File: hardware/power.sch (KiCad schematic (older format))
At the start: 22 parts

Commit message: Almost finished layout
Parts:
- removed D? (x3): 1N4002, symbol D_Small
- added D4, D5, D6: S1KB-13-F, Diodes_SMD:SMB_Standard, symbol D_Small
- added D7: LED_5V, Connectors_Molex:Molex_KK-6410-02_02x2.54mm_Straight, symbol Led_Small
- added D8: LED_3V3, Connectors_Molex:Molex_KK-6410-02_02x2.54mm_Straight, symbol Led_Small
- added R35: 270R, Resistors_SMD:R_1210, symbol R_Small
- added R36: 180R, Resistors_SMD:R_1210, symbol R_Small
- C34, C37, C38, C41: renamed from C?; value 47u -> 10u; footprint (none) -> Capacitors_ThroughHole:C_Radial_D5_L11_P2
- C35, C39: renamed from C?; footprint (none) -> Capacitors_SMD:C_1210
- C36, C40: renamed from C?; value ? -> 10u; footprint (none) -> Capacitors_ThroughHole:C_Radial_D5_L11_P2
- D3: renamed from D?; value 1N4002 -> S1KB-13-F; footprint (none) -> Diodes_SMD:SMB_Standard
- R31, R32, R33, R34: renamed from R?; footprint (none) -> Resistors_SMD:R_1210
- U4, U5: renamed from U?; footprint TO_SOT_Packages_THT:TO-220_Neutral123_Vertical_LargePads -> TO_SOT_Packages_THT:TO-220_Neutral123_Vertical_MountedFromLS
- gave numbers to parts that had none: 4
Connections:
- net 3V3A: now also D5.2 (A), D6.1 (K), D8.2 (A)
- net 5VA: now also D4.1 (K), D5.1 (K), D7.2 (A)
- net GND: now also R35.2, R36.2
- net at C40.1, R33.2, R34.1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: now also D6.2 (A)
- net at C36.1, R31.2, R32.1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: now also D4.2 (A)
- new net: D7.1 (K), R35.1
- new net: D8.1 (K), R36.1

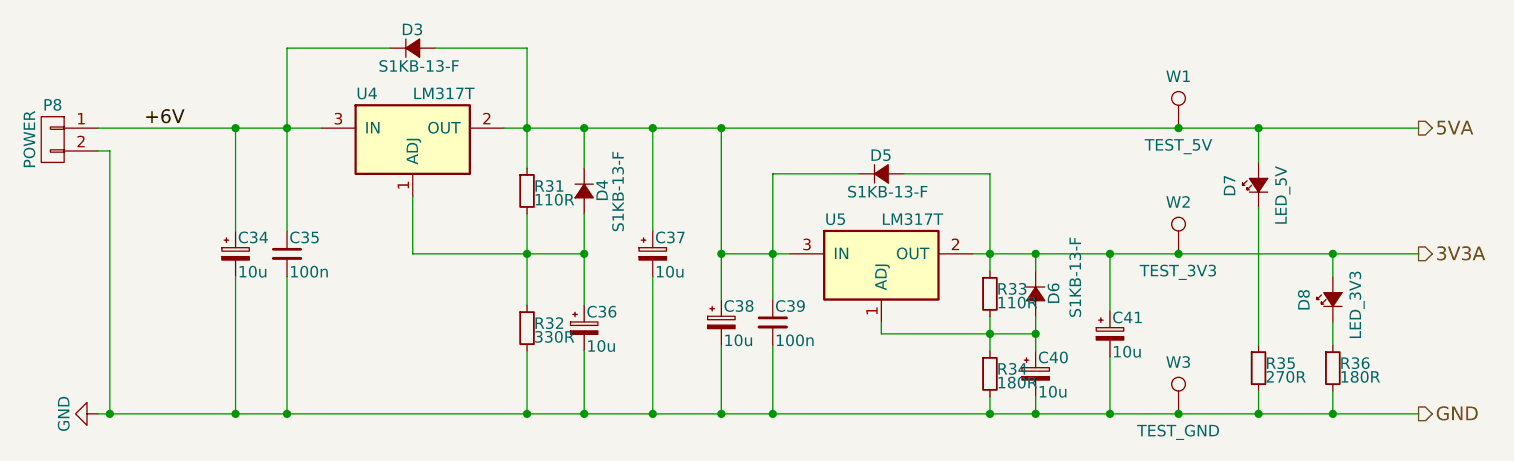
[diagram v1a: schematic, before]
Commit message: Move labels, replace some SMB diodes with SMA, final tweaks
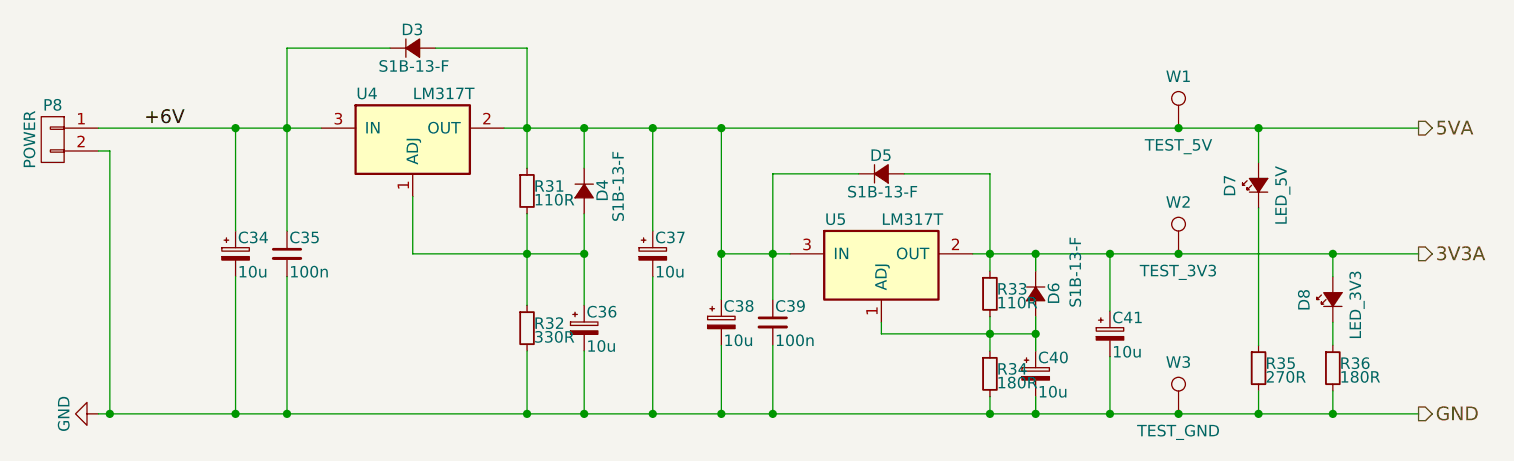
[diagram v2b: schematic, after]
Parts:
- D3, D4, D5, D6: value S1KB-13-F -> S1B-13-F; footprint Diodes_SMD:SMB_Standard -> Diodes_SMD:SMA_Standard
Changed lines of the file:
@@
 P 4750 2800
 F 0 "D3" H 4700 2880 50  0000 L CNN
-F 1 "S1KB-13-F" H 4600 2720 50  0000 L CNN
-F 2 "Diodes_SMD:SMB_Standard" V 4750 2800 50  0001 C CNN
+F 1 "S1B-13-F" H 4600 2720 50  0000 L CNN
+F 2 "Diodes_SMD:SMA_Standard" V 4750 2800 50  0001 C CNN
 F 3 "" V 4750 2800 50  0000 C CNN
 	1    4750 2800
@@
 P 6800 3350
 F 0 "D5" H 6750 3430 50  0000 L CNN
-F 1 "S1KB-13-F" H 6650 3270 50  0000 L CNN
-F 2 "Diodes_SMD:SMB_Standard" V 6800 3350 50  0001 C CNN
+F 1 "S1B-13-F" H 6650 3270 50  0000 L CNN
+F 2 "Diodes_SMD:SMA_Standard" V 6800 3350 50  0001 C CNN
 F 3 "" V 6800 3350 50  0000 C CNN
 	1    6800 3350
@@
 P 5500 3425
 F 0 "D4" H 5450 3505 50  0000 L CNN
-F 1 "S1KB-13-F" H 5325 3575 50  0000 L CNN
-F 2 "Diodes_SMD:SMB_Standard" V 5500 3425 50  0001 C CNN
+F 1 "S1B-13-F" H 5325 3575 50  0000 L CNN
+F 2 "Diodes_SMD:SMA_Standard" V 5500 3425 50  0001 C CNN
 F 3 "" V 5500 3425 50  0000 C CNN
 	1    5500 3425
@@
 P 7475 3875
 F 0 "D6" H 7425 3955 50  0000 L CNN
-F 1 "S1KB-13-F" H 7225 4050 50  0000 L CNN
-F 2 "Diodes_SMD:SMB_Standard" V 7475 3875 50  0001 C CNN
+F 1 "S1B-13-F" H 7225 4050 50  0000 L CNN
+F 2 "Diodes_SMD:SMA_Standard" V 7475 3875 50  0001 C CNN
 F 3 "" V 7475 3875 50  0000 C CNN
 	1    7475 3875

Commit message: Move LM317 regulator footprints to underside; final tweaks
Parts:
- U4, U5: footprint TO_SOT_Packages_THT:TO-220_Neutral123_Vertical_MountedFromLS -> TO_SOT_Packages_THT:TO-220_Neutral123_Vertical
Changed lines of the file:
@@
 F 0 "U5" H 6600 3950 50  0000 C CNN
 F 1 "LM317T" H 6800 3950 50  0000 L CNN
-F 2 "TO_SOT_Packages_THT:TO-220_Neutral123_Vertical_MountedFromLS" H 6800 3850 50  0001 C CIN
+F 2 "TO_SOT_Packages_THT:TO-220_Neutral123_Vertical" H 6800 3850 50  0001 C CIN
 F 3 "" H 6800 3750 50  0000 C CNN
 	1    6800 3750
@@
 F 0 "U4" H 4550 3400 50  0000 C CNN
 F 1 "LM317T" H 4750 3400 50  0000 L CNN
-F 2 "TO_SOT_Packages_THT:TO-220_Neutral123_Vertical_MountedFromLS" H 4750 3300 50  0001 C CIN
+F 2 "TO_SOT_Packages_THT:TO-220_Neutral123_Vertical" H 4750 3300 50  0001 C CIN
 F 3 "" H 4750 3200 50  0000 C CNN
 	1    4750 3200

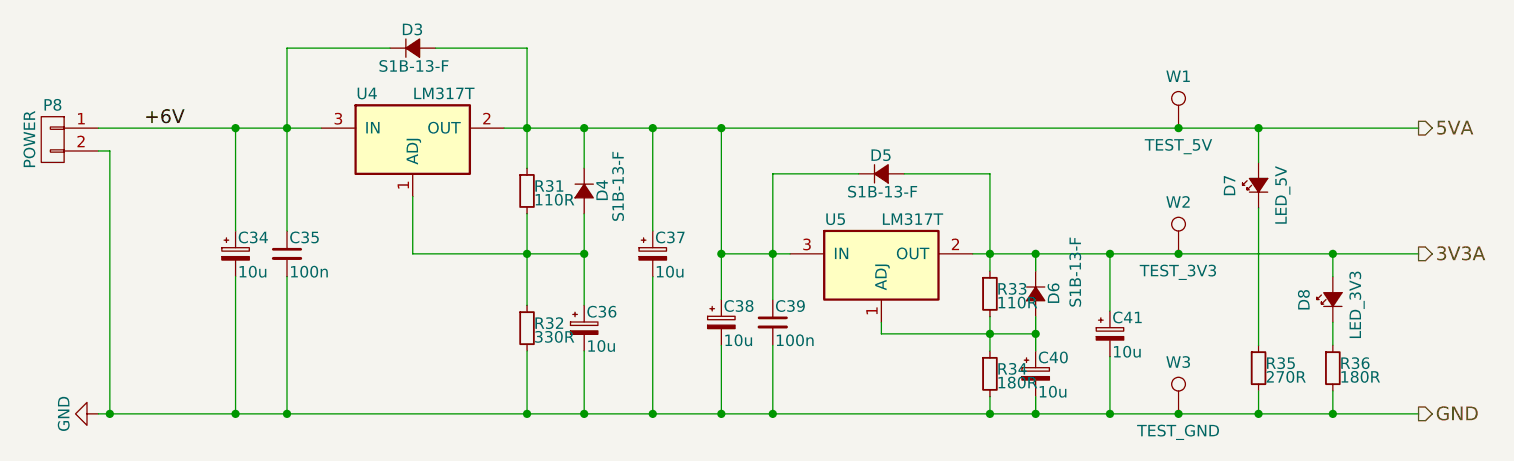
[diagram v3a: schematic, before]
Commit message: Revision of board to address issues
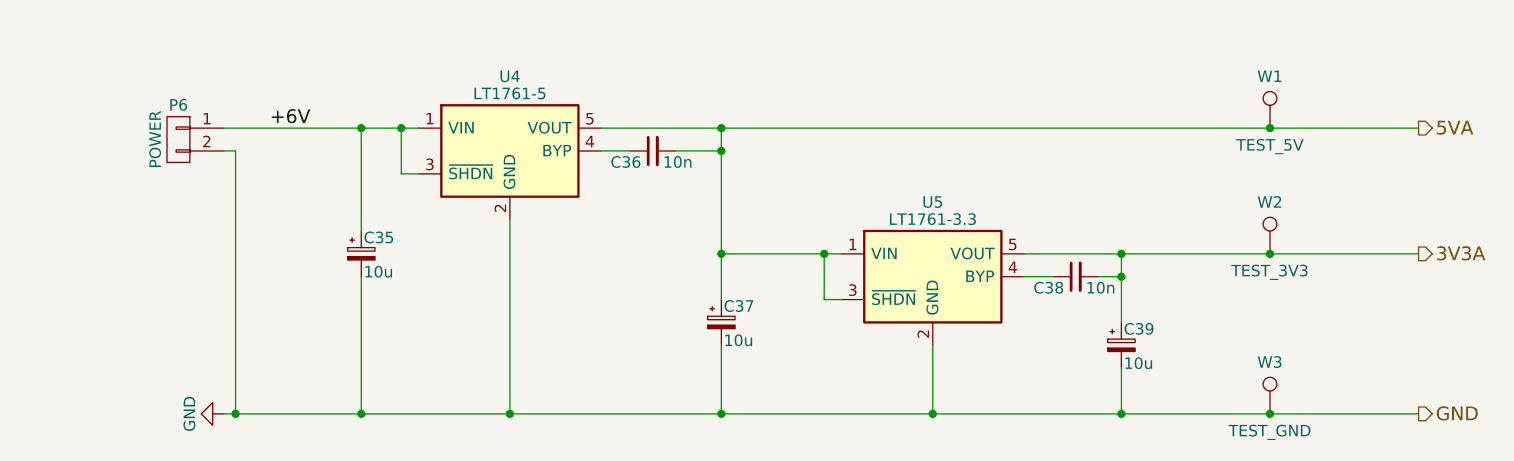
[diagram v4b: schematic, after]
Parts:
- removed C35, C39: 100n, Capacitors_SMD:C_1210, symbol C_Small
- removed C36, C37, C40, C41: 10u, Capacitors_ThroughHole:C_Radial_D5_L11_P2, symbol CP_Small
- removed D3, D4, D5, D6: S1B-13-F, Diodes_SMD:SMA_Standard, symbol D_Small
- removed D7: LED_5V, Connectors_Molex:Molex_KK-6410-02_02x2.54mm_Straight, symbol Led_Small
- removed D8: LED_3V3, Connectors_Molex:Molex_KK-6410-02_02x2.54mm_Straight, symbol Led_Small
- removed R31, R33: 110R, Resistors_SMD:R_1210, symbol R_Small
- removed R32: 330R, Resistors_SMD:R_1210, symbol R_Small
- removed R34, R36: 180R, Resistors_SMD:R_1210, symbol R_Small
- removed R35: 270R, Resistors_SMD:R_1210, symbol R_Small
- removed U4, U5: LM317T, TO_SOT_Packages_THT:TO-220_Neutral123_Vertical, symbol LM317T
- added C36, C38: 10n, Capacitors_SMD:C_1206, symbol C_Small
- added C39: 10u, Capacitors_ThroughHole:C_Radial_D5_L11_P2, symbol CP_Small
- added U4: LT1761-5, TO_SOT_Packages_SMD:SOT-23-5, symbol LT1761-5
- added U5: LT1761-3.3, TO_SOT_Packages_SMD:SOT-23-5, symbol LT1761-3.3
- renumbered C34 to C35, C38 to C37, P8 to P6
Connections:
- net +6V: now also U4.1 (VIN), U4.3 (~SHDN)
- net 3V3A: now also C38.2, C39.1, U5.5 (VOUT)
- net 5VA: now also C36.2, U4.5 (VOUT), U5.1 (VIN), U5.3 (~SHDN)
- net GND: now also C39.2, U4.2 (GND), U5.2 (GND)
- new net: C36.1, U4.4 (BYP)
- new net: C38.1, U5.4 (BYP)
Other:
- moved on the sheet: C35, P6, W1, W2, W3

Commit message: New revision to board
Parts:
- P1: renamed from P6; footprint Terminal_Blocks:TerminalBlock_Pheonix_MKDS1.5-2pol -> Connectors_Molex:Molex_KK-6410-02_02x2.54mm_Straight
- renumbered C35 to C1, C36 to C2, C37 to C3, C38 to C4, C39 to C5, U4 to U1, U5 to U2
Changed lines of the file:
@@
 LIBS:Sensors_Bosch
 LIBS:cetus
+LIBS:LDRs_NSL
 LIBS:environment-sensor-cache
 EELAYER 25 0
@@
 $Descr A4 11693 8268
 encoding utf-8
-Sheet 5 5
+Sheet 2 5
 Title ""
 Date ""
@@
 5VA
 $Comp
-L CONN_01X02 P6
+L CONN_01X02 P1
 U 1 1 58F70F15
 P 3725 3200
-F 0 "P6" H 3725 3350 50  0000 C CNN
+F 0 "P1" H 3725 3350 50  0000 C CNN
 F 1 "POWER" V 3825 3200 50  0000 C CNN
-F 2 "Terminal_Blocks:TerminalBlock_Pheonix_MKDS1.5-2pol" H 3725 3200 50  0001 C CNN
+F 2 "Connectors_Molex:Molex_KK-6410-02_02x2.54mm_Straight" H 3725 3200 50  0001 C CNN
 F 3 "" H 3725 3200 50  0000 C CNN
 	1    3725 3200
@@
 +6V
 $Comp
-L CP_Small C35
+L CP_Small C1
 U 1 1 58F717C2
 P 4525 3700
-F 0 "C35" H 4535 3770 50  0000 L CNN
+F 0 "C1" H 4535 3770 50  0000 L CNN
 F 1 "10u" H 4535 3620 50  0000 L CNN
 F 2 "Capacitors_ThroughHole:C_Radial_D5_L11_P2" H 4525 3700 50  0001 C CNN
@@
 $EndComp
 $Comp
-L CP_Small C37
+L CP_Small C3
 U 1 1 58F72F88
 P 6100 4000
-F 0 "C37" H 6110 4070 50  0000 L CNN
+F 0 "C3" H 6110 4070 50  0000 L CNN
 F 1 "10u" H 6110 3920 50  0000 L CNN
 F 2 "Capacitors_ThroughHole:C_Radial_D5_L11_P2" H 6100 4000 50  0001 C CNN
@@
 $EndComp
 $Comp
-L LT1761-5 U4
+L LT1761-5 U1
 U 1 1 594B0D60
 P 5175 3250
-F 0 "U4" H 5175 3575 50  0000 C CNN
+F 0 "U1" H 5175 3575 50  0000 C CNN
 F 1 "LT1761-5" H 5175 3500 50  0000 C CNN
 F 2 "TO_SOT_Packages_SMD:SOT-23-5" H 5225 3000 50  0001 L CNN
@@
 Connection ~ 4700 3150
 $Comp
-L C_Small C36
+L C_Small C2
 U 1 1 594B3D4A
 P 5800 3250
-F 0 "C36" V 5750 3300 50  0000 L CNN
+F 0 "C2" V 5750 3300 50  0000 L CNN
 F 1 "10n" V 5750 3075 50  0000 L CNN
 F 2 "Capacitors_SMD:C_1206" H 5800 3250 50  0001 C CNN
@@
 Connection ~ 6100 3250
 $Comp
-L LT1761-3.3 U5
+L LT1761-3.3 U2
 U 1 1 594B84C6
 P 7025 3800
-F 0 "U5" H 7025 4125 50  0000 C CNN
+F 0 "U2" H 7025 4125 50  0000 C CNN
 F 1 "LT1761-3.3" H 7025 4050 50  0000 C CNN
 F 2 "TO_SOT_Packages_SMD:SOT-23-5" H 7075 3550 50  0001 L CNN
@@
 Connection ~ 7025 4400
 $Comp
-L C_Small C38
+L C_Small C4
 U 1 1 594B89E1
 P 7650 3800
-F 0 "C38" V 7600 3850 50  0000 L CNN
+F 0 "C4" V 7600 3850 50  0000 L CNN
 F 1 "10n" V 7600 3625 50  0000 L CNN
 F 2 "Capacitors_SMD:C_1206" H 7650 3800 50  0001 C CNN
@@
 Connection ~ 7850 3700
 $Comp
-L CP_Small C39
+L CP_Small C5
 U 1 1 594B9BFC
 P 7850 4100
-F 0 "C39" H 7860 4170 50  0000 L CNN
+F 0 "C5" H 7860 4170 50  0000 L CNN
 F 1 "10u" H 7860 4020 50  0000 L CNN
 F 2 "Capacitors_ThroughHole:C_Radial_D5_L11_P2" H 7850 4100 50  0001 C CNN
@@
 	7850 4200 7850 4400
 Connection ~ 7850 4400
+Wire Wire Line
+	3975 2975 3975 3150
+Connection ~ 3975 3150
+$Comp
+L PWR_FLAG #FLG02
+U 1 1 59DCF846
+P 3975 2975
+F 0 "#FLG02" H 3975 3070 50  0001 C CNN
+F 1 "PWR_FLAG" H 3975 3155 50  0000 C CNN
+F 2 "" H 3975 2975 50  0000 C CNN
+F 3 "" H 3975 2975 50  0000 C CNN
+	1    3975 2975
+	1    0    0    -1
+$EndComp
 $EndSCHEMATC

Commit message: Added some part numbers to the schematic
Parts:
- P1: MPN1 (none) -> 22-27-2021; Manufacturer1 (none) -> Molex; SKU1 (none) -> 483-8461; Vendor1 (none) -> RS
- U1: MPN1 (none) -> LT1761ES5-5#TRMPBF; Manufacturer1 (none) -> Linear Technology; SKU1 (none) -> 411-895; Vendor1 (none) -> RS
- U2: MPN1 (none) -> LT1761ES5-3.3#TRMPBF; Manufacturer1 (none) -> Linear Technology; SKU1 (none) -> 396-471; Vendor1 (none) -> RS
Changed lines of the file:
@@
 F 2 "Connectors_Molex:Molex_KK-6410-02_02x2.54mm_Straight" H 3725 3200 50  0001 C CNN
 F 3 "" H 3725 3200 50  0000 C CNN
+F 4 "Molex" H 3725 3200 60  0001 C CNN "Manufacturer1"
+F 5 "22-27-2021" H 3725 3200 60  0001 C CNN "MPN1"
+F 6 "RS" H 3725 3200 60  0001 C CNN "Vendor1"
+F 7 "483-8461" H 3725 3200 60  0001 C CNN "SKU1"
 	1    3725 3200
 	-1   0    0    -1
@@
 F 2 "TO_SOT_Packages_SMD:SOT-23-5" H 5225 3000 50  0001 L CNN
 F 3 "" H 5175 3250 50  0000 C CNN
+F 4 "Linear Technology" H 5175 3250 60  0001 C CNN "Manufacturer1"
+F 5 "LT1761ES5-5#TRMPBF" H 5175 3250 60  0001 C CNN "MPN1"
+F 6 "RS" H 5175 3250 60  0001 C CNN "Vendor1"
+F 7 "411-895" H 5175 3250 60  0001 C CNN "SKU1"
 	1    5175 3250
 	1    0    0    -1
@@
 F 2 "TO_SOT_Packages_SMD:SOT-23-5" H 7075 3550 50  0001 L CNN
 F 3 "" H 7025 3800 50  0000 C CNN
+F 4 "Linear Technology" H 7025 3800 60  0001 C CNN "Manufacturer1"
+F 5 "LT1761ES5-3.3#TRMPBF" H 7025 3800 60  0001 C CNN "MPN1"
+F 6 "RS" H 7025 3800 60  0001 C CNN "Vendor1"
+F 7 "396-471" H 7025 3800 60  0001 C CNN "SKU1"
 	1    7025 3800
 	1    0    0    -1
